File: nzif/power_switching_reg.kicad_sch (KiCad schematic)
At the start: 50 parts, among them U1101 LT8330xS6, U1102 ADP2303ARDZ, U1103 ADP2303ARDZ, U1104 ADP2303ARDZ

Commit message: erc updates
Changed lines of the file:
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@@
 		(in_pos_files yes)
 		(dnp no)
+		(fields_autoplaced yes)
 		(property "Reference" "R1106"
-			(at 195.58 213.36 0)
+			(at 201.93 213.3599 0)
 			(show_name no)
 			(do_not_autoplace no)
@@
 		)
 		(property "Value" "1M"
-			(at 200.66 214.376 0)
+			(at 201.93 215.8999 0)
 			(show_name no)
 			(do_not_autoplace no)
@@
 		(in_pos_files yes)
 		(dnp no)
+		(fields_autoplaced yes)
 		(property "Reference" "R1107"
-			(at 195.58 220.98 0)
-			(show_name no)
-			(do_not_autoplace no)
-			(effects
-				(font
-					(size 1.27 1.27)
-				)
-				(justify left)
+			(at 196.85 220.9799 0)
+			(show_name no)
+			(do_not_autoplace no)
+			(effects
+				(font
+					(size 1.27 1.27)
+				)
+				(justify right)
 			)
 		)
 		(property "Value" "191k"
-			(at 200.914 222.504 0)
-			(show_name no)
-			(do_not_autoplace no)
-			(effects
-				(font
-					(size 1.27 1.27)
-				)
-				(justify left)
-			)
-		)
+			(at 196.85 223.5199 0)
+			(show_name no)
+			(do_not_autoplace no)
+			(effects
+				(font
+					(size 1.27 1.27)
+				)
+				(justify right)
+			)
+		)

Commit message: added footprints for Rs and Cs
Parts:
- C1101, C1102, C1103, C1104, C1105, C1106, C1107, C1108, C1109, C1110, C1111, C1112, C1113, C1114, C1115, C1116, C1117, C1118, C1119, C1120: footprint Capacitor_SMD:C_0603_1608Metric -> Capacitor_SMD:C_0402_1005Metric_Pad0.74x0.62mm_HandSolder
- D1104: footprint (none) -> Connector_Coaxial:SMA_Amphenol_901-143_Horizontal
- R1101, R1102, R1103, R1104, R1105, R1106, R1107, R1108, R1109, R1110, R1111, R1112, R1113: footprint Resistor_SMD:R_0603_1608Metric -> Resistor_SMD:R_0402_1005Metric_Pad0.72x0.64mm_HandSolder
- TP1201, TP1202, TP1203, TP1204: footprint (none) -> Connector_PinHeader_1.27mm:PinHeader_1x01_P1.27mm_Vertical
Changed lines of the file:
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@@
 			)
 		)
-		(property "Footprint" ""
+		(property "Footprint" "Connector_Coaxial:SMA_Amphenol_901-143_Horizontal"
 			(at 175.895 193.04 0)
 			(hide yes)
@@
 			)
 		)
-		(property "Footprint" "Resistor_SMD:R_0603_1608Metric"
+		(property "Footprint" "Resistor_SMD:R_0402_1005Metric_Pad0.72x0.64mm_HandSolder"
 			(at 227.33 139.7 0)
 			(hide yes)
@@
 			)
 		)
-		(property "Footprint" "Capacitor_SMD:C_0603_1608Metric"
+		(property "Footprint" "Capacitor_SMD:C_0402_1005Metric_Pad0.74x0.62mm_HandSolder"
 			(at 160.02 215.9 0)
 			(hide yes)
@@
 			)
 		)
-		(property "Footprint" "Capacitor_SMD:C_0603_1608Metric"
+		(property "Footprint" "Capacitor_SMD:C_0402_1005Metric_Pad0.74x0.62mm_HandSolder"
 			(at 217.17 214.63 0)
 			(hide yes)
@@
 			)
 		)
-		(property "Footprint" "Capacitor_SMD:C_0603_1608Metric"
+		(property "Footprint" "Capacitor_SMD:C_0402_1005Metric_Pad0.74x0.62mm_HandSolder"
 			(at 121.92 31.75 0)
 			(hide yes)
@@
 			)
 		)
-		(property "Footprint" "Resistor_SMD:R_0603_1608Metric"
+		(property "Footprint" "Resistor_SMD:R_0402_1005Metric_Pad0.72x0.64mm_HandSolder"
 			(at 130.81 36.83 0)
 			(hide yes)
@@
 			)
 		)
-		(property "Footprint" "Resistor_SMD:R_0603_1608Metric"
+		(property "Footprint" "Resistor_SMD:R_0402_1005Metric_Pad0.72x0.64mm_HandSolder"
 			(at 223.52 40.64 0)
 			(hide yes)
@@
 			)
 		)
-		(property "Footprint" "Resistor_SMD:R_0603_1608Metric"
+		(property "Footprint" "Resistor_SMD:R_0402_1005Metric_Pad0.72x0.64mm_HandSolder"
 			(at 227.33 82.55 0)
 			(hide yes)
@@
 			)
 		)
-		(property "Footprint" "Resistor_SMD:R_0603_1608Metric"
+		(property "Footprint" "Resistor_SMD:R_0402_1005Metric_Pad0.72x0.64mm_HandSolder"
 			(at 223.52 33.02 0)
 			(hide yes)
@@
 			)
 		)
-		(property "Footprint" "Capacitor_SMD:C_0603_1608Metric"
+		(property "Footprint" "Capacitor_SMD:C_0402_1005Metric_Pad0.74x0.62mm_HandSolder"
 			(at 194.31 34.29 0)
 			(hide yes)
@@
 			)
 		)
-		(property "Footprint" "Resistor_SMD:R_0603_1608Metric"
+		(property "Footprint" "Resistor_SMD:R_0402_1005Metric_Pad0.72x0.64mm_HandSolder"
 			(at 134.62 135.89 0)
 			(hide yes)
@@
 			)
 		)
-		(property "Footprint" "Resistor_SMD:R_0603_1608Metric"
+		(property "Footprint" "Resistor_SMD:R_0402_1005Metric_Pad0.72x0.64mm_HandSolder"
 			(at 199.39 214.63 0)
 			(hide yes)
@@
 			)
 		)
-		(property "Footprint" "Capacitor_SMD:C_0603_1608Metric"
+		(property "Footprint" "Capacitor_SMD:C_0402_1005Metric_Pad0.74x0.62mm_HandSolder"
 			(at 209.55 83.82 0)
 			(hide yes)
@@
 			)
 		)
-		(property "Footprint" "Capacitor_SMD:C_0603_1608Metric"
+		(property "Footprint" "Capacitor_SMD:C_0402_1005Metric_Pad0.74x0.62mm_HandSolder"
 			(at 124.46 190.5 0)
 			(hide yes)
@@
 			)
 		)
-		(property "Footprint" "Capacitor_SMD:C_0603_1608Metric"
+		(property "Footprint" "Capacitor_SMD:C_0402_1005Metric_Pad0.74x0.62mm_HandSolder"
 			(at 171.45 81.28 0)
 			(hide yes)
@@
 			)
 		)
-		(property "Footprint" "Capacitor_SMD:C_0603_1608Metric"
+		(property "Footprint" "Capacitor_SMD:C_0402_1005Metric_Pad0.74x0.62mm_HandSolder"
 			(at 167.64 31.75 0)
 			(hide yes)
@@
 			)
 		)
-		(property "Footprint" "Capacitor_SMD:C_0603_1608Metric"
+		(property "Footprint" "Capacitor_SMD:C_0402_1005Metric_Pad0.74x0.62mm_HandSolder"
 			(at 182.88 34.29 0)
 			(hide yes)
@@
 			)
 		)
-		(property "Footprint" ""
+		(property "Footprint" "Connector_PinHeader_1.27mm:PinHeader_1x01_P1.27mm_Vertical"
 			(at 205.74 20.32 0)
 			(hide yes)
@@
 			)
 		)
-		(property "Footprint" "Resistor_SMD:R_0603_1608Metric"
+		(property "Footprint" "Resistor_SMD:R_0402_1005Metric_Pad0.72x0.64mm_HandSolder"
 			(at 199.39 222.25 0)
 			(hide yes)
@@
 			)
 		)
-		(property "Footprint" "Resistor_SMD:R_0603_1608Metric"
+		(property "Footprint" "Resistor_SMD:R_0402_1005Metric_Pad0.72x0.64mm_HandSolder"
 			(at 227.33 90.17 0)
 			(hide yes)
@@
 			)
 		)
-		(property "Footprint" "Capacitor_SMD:C_0603_1608Metric"
+		(property "Footprint" "Capacitor_SMD:C_0402_1005Metric_Pad0.74x0.62mm_HandSolder"
 			(at 205.74 34.29 0)
 			(hide yes)
@@
 			)
 		)
-		(property "Footprint" "Capacitor_SMD:C_0603_1608Metric"
+		(property "Footprint" "Capacitor_SMD:C_0402_1005Metric_Pad0.74x0.62mm_HandSolder"
 			(at 162.56 184.15 0)
 			(hide yes)
@@
 			)
 		)
-		(property "Footprint" "Capacitor_SMD:C_0603_1608Metric"
+		(property "Footprint" "Capacitor_SMD:C_0402_1005Metric_Pad0.74x0.62mm_HandSolder"
 			(at 186.69 133.35 0)
 			(hide yes)
@@
 			)
 		)
-		(property "Footprint" "Capacitor_SMD:C_0603_1608Metric"
+		(property "Footprint" "Capacitor_SMD:C_0402_1005Metric_Pad0.74x0.62mm_HandSolder"
 			(at 198.12 133.35 0)
 			(hide yes)
@@
 			)
 		)
-		(property "Footprint" "Capacitor_SMD:C_0603_1608Metric"
+		(property "Footprint" "Capacitor_SMD:C_0402_1005Metric_Pad0.74x0.62mm_HandSolder"
 			(at 171.45 130.81 0)
 			(hide yes)
@@
 			)
 		)
-		(property "Footprint" ""
+		(property "Footprint" "Connector_PinHeader_1.27mm:PinHeader_1x01_P1.27mm_Vertical"
 			(at 208.28 120.65 0)
 			(hide yes)
@@
 			)
 		)
-		(property "Footprint" ""
+		(property "Footprint" "Connector_PinHeader_1.27mm:PinHeader_1x01_P1.27mm_Vertical"
 			(at 203.2 168.91 0)
 			(hide yes)
@@
 			)
 		)
-		(property "Footprint" "Capacitor_SMD:C_0603_1608Metric"
+		(property "Footprint" "Capacitor_SMD:C_0402_1005Metric_Pad0.74x0.62mm_HandSolder"
 			(at 125.73 81.28 0)
 			(hide yes)
@@
 			)
 		)
-		(property "Footprint" ""
+		(property "Footprint" "Connector_PinHeader_1.27mm:PinHeader_1x01_P1.27mm_Vertical"
 			(at 207.01 69.85 0)
 			(hide yes)
@@
 			)
 		)
-		(property "Footprint" "Capacitor_SMD:C_0603_1608Metric"
+		(property "Footprint" "Capacitor_SMD:C_0402_1005Metric_Pad0.74x0.62mm_HandSolder"
 			(at 209.55 133.35 0)
 			(hide yes)
@@
 			)
 		)
-		(property "Footprint" "Capacitor_SMD:C_0603_1608Metric"
+		(property "Footprint" "Capacitor_SMD:C_0402_1005Metric_Pad0.74x0.62mm_HandSolder"
 			(at 186.69 83.82 0)
 			(hide yes)
@@
 			)
 		)
-		(property "Footprint" "Capacitor_SMD:C_0603_1608Metric"
+		(property "Footprint" "Capacitor_SMD:C_0402_1005Metric_Pad0.74x0.62mm_HandSolder"
 			(at 198.12 83.82 0)
 			(hide yes)
@@
 			)
 		)
-		(property "Footprint" "Capacitor_SMD:C_0603_1608Metric"
+		(property "Footprint" "Capacitor_SMD:C_0402_1005Metric_Pad0.74x0.62mm_HandSolder"
 			(at 125.73 130.81 0)
 			(hide yes)
@@
 			)
 		)
-		(property "Footprint" "Capacitor_SMD:C_0603_1608Metric"
+		(property "Footprint" "Capacitor_SMD:C_0402_1005Metric_Pad0.74x0.62mm_HandSolder"
 			(at 213.36 190.5 0)
 			(hide yes)
@@
 			)
 		)
-		(property "Footprint" "Resistor_SMD:R_0603_1608Metric"
+		(property "Footprint" "Resistor_SMD:R_0402_1005Metric_Pad0.72x0.64mm_HandSolder"
 			(at 227.33 132.08 0)
 			(hide yes)
@@
 			)
 		)
-		(property "Footprint" "Resistor_SMD:R_0603_1608Metric"
+		(property "Footprint" "Resistor_SMD:R_0402_1005Metric_Pad0.72x0.64mm_HandSolder"
 			(at 134.62 86.36 0)
 			(hide yes)
@@
 			)
 		)
-		(property "Footprint" "Resistor_SMD:R_0603_1608Metric"
+		(property "Footprint" "Resistor_SMD:R_0402_1005Metric_Pad0.72x0.64mm_HandSolder"
 			(at 111.76 203.2 0)
 			(hide yes)
@@
 			)
 		)
-		(property "Footprint" "Resistor_SMD:R_0603_1608Metric"
+		(property "Footprint" "Resistor_SMD:R_0402_1005Metric_Pad0.72x0.64mm_HandSolder"
 			(at 111.76 210.82 0)
 			(hide yes)
@@
 		)
 	)
-	(embedded_fonts no)
 )

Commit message: updates from schematic review
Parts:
- C1110, C1111, C1112, C1113, C1114, C1115, C1116, C1117, C1118: value 47u 6.3V -> 47u 16V
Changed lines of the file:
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@@
 			)
 		)
-		(property "Value" "47u 6.3V"
+		(property "Value" "47u 16V"
 			(at 195.834 36.068 0)
 			(show_name no)
@@
 			)
 		)
-		(property "Value" "47u 6.3V"
+		(property "Value" "47u 16V"
 			(at 211.074 85.598 0)
 			(show_name no)
@@
 			)
 		)
-		(property "Value" "47u 6.3V"
+		(property "Value" "47u 16V"
 			(at 184.404 36.068 0)
 			(show_name no)
@@
 			)
 		)
-		(property "Value" "47u 6.3V"
+		(property "Value" "47u 16V"
 			(at 207.264 36.068 0)
 			(show_name no)
@@
 			)
 		)
-		(property "Value" "47u 6.3V"
+		(property "Value" "47u 16V"
 			(at 188.214 135.128 0)
 			(show_name no)
@@
 			)
 		)
-		(property "Value" "47u 6.3V"
+		(property "Value" "47u 16V"
 			(at 199.644 135.128 0)
 			(show_name no)
@@
 			)
 		)
-		(property "Value" "47u 6.3V"
+		(property "Value" "47u 16V"
 			(at 211.074 135.128 0)
 			(show_name no)
@@
 			)
 		)
-		(property "Value" "47u 6.3V"
+		(property "Value" "47u 16V"
 			(at 188.214 85.598 0)
 			(show_name no)
@@
 			)
 		)
-		(property "Value" "47u 6.3V"
+		(property "Value" "47u 16V"
 			(at 199.644 85.598 0)
 			(show_name no)
@@
 		(in_pos_files yes)
 		(dnp no)
-		(fields_autoplaced yes)
 		(property "Reference" "L1101"
 			(at 148.59 177.8 90)
@@
 		)
 		(property "Value" "2.7u Wurth WE-TDC 8018 74489430027"
-			(at 148.59 180.34 90)
+			(at 149.098 173.736 90)
 			(show_name no)
 			(do_not_autoplace no)

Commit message: assigned missing footprints
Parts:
- L1101: footprint (none) -> TerminalBlock:TerminalBlock_MaiXu_MX126-5.0-02P_1x02_P5.00mm
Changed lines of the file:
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@@
 			)
 		)
-		(property "Footprint" ""
+		(property "Footprint" "TerminalBlock:TerminalBlock_MaiXu_MX126-5.0-02P_1x02_P5.00mm"
 			(at 148.59 184.15 0)
 			(hide yes)

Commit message: preparing pcb
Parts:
- L1101: value 2.7u Wurth WE-TDC 8018 74489430027 -> 2.7u; footprint TerminalBlock:TerminalBlock_MaiXu_MX126-5.0-02P_1x02_P5.00mm -> (none)
- L1105: value 2.7u Wurth WE-TDC 8018 74489430027 -> 2.7u
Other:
- note added: "Wurth WE-TDC 8018 74489430027"
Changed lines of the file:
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@@
 		(company "Andy McCann KA3KAF and Doug McCann KA3KAG")
 	)
+	(text "Wurth WE-TDC 8018 74489430027"
+		(exclude_from_sim no)
+		(at 172.974 173.228 0)
+		(effects
+			(font
+				(size 1.27 1.27)
+			)
+		)
+	)
 	(text "These passive values all need to be properly calculated using the datasheet. \nThe target voltages are 8V, 6V, 4V"
 		(exclude_from_sim no)
@@
 			)
 		)
-		(property "Value" "2.7u Wurth WE-TDC 8018 74489430027"
+		(property "Value" "2.7u"
 			(at 191.77 180.34 90)
 			(show_name no)
@@
 			)
 		)
-		(property "Datasheet" ""
+		(property "Datasheet" "https://www.digikey.com/en/products/detail/w%C3%BCrth-elektronik/74489430027/2445599"
 			(at 191.77 184.15 0)
 			(hide yes)
@@
 			)
 		)
-		(property "Value" "2.7u Wurth WE-TDC 8018 74489430027"
+		(property "Value" "2.7u"
 			(at 149.098 173.736 90)
 			(show_name no)
@@
 			)
 		)
-		(property "Footprint" "TerminalBlock:TerminalBlock_MaiXu_MX126-5.0-02P_1x02_P5.00mm"
+		(property "Footprint" ""
 			(at 148.59 184.15 0)
 			(hide yes)
@@
 			)
 		)
-		(property "Datasheet" ""
+		(property "Datasheet" "https://www.digikey.com/en/products/detail/w%C3%BCrth-elektronik/74489430027/2445599"
 			(at 148.59 184.15 0)
 			(hide yes)

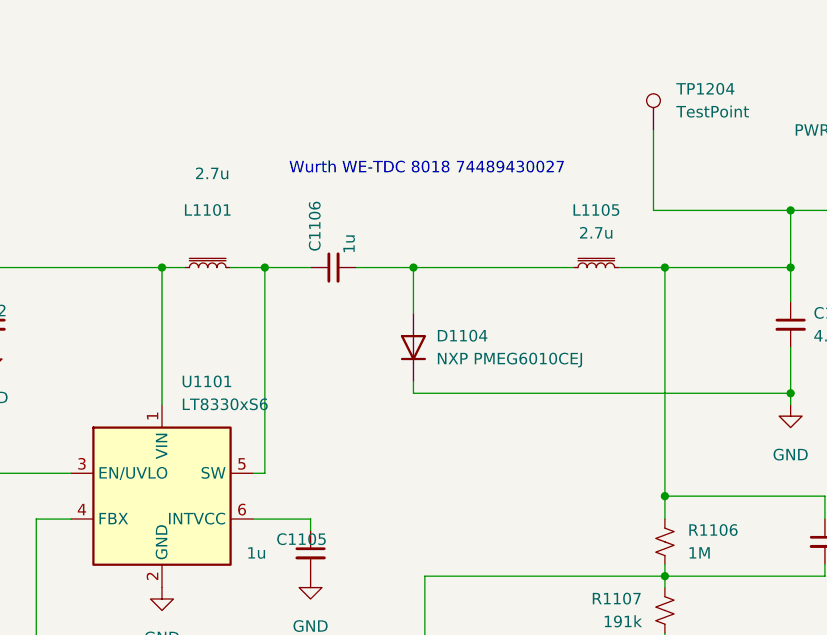
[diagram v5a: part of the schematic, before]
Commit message: added footprints for L that goes with LT8330
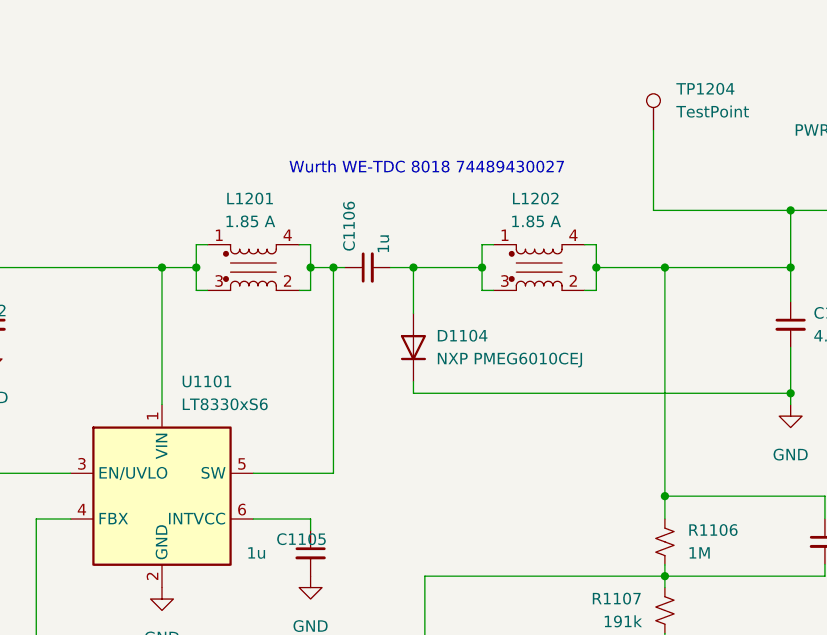
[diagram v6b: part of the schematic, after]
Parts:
- removed L1101, L1105: 2.7u, symbol Device:L_Iron_Small
- added L1201, L1202: 8018_74489430027, nzif_footprints:L_Wurth_WE-TDC-8018, symbol nzif_radio_symbol_library:8018_74489430027
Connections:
- net -5V_SW: now also L1202.2, L1202.4
- net MAIN: now also L1201.1, L1201.3
- net at C1106.2, D1104.2 (A): now also L1202.1, L1202.3
- net at C1106.1, U1101.5 (SW): now also L1201.2, L1201.4
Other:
- moved on the sheet: C1106
